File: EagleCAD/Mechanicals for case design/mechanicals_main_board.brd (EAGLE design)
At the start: 77 x 46.5 mm, 65 parts, among them Q1 DMC2700, U3 LM3676, U4 STM32F072-LQFP48, X1 32.768kHz

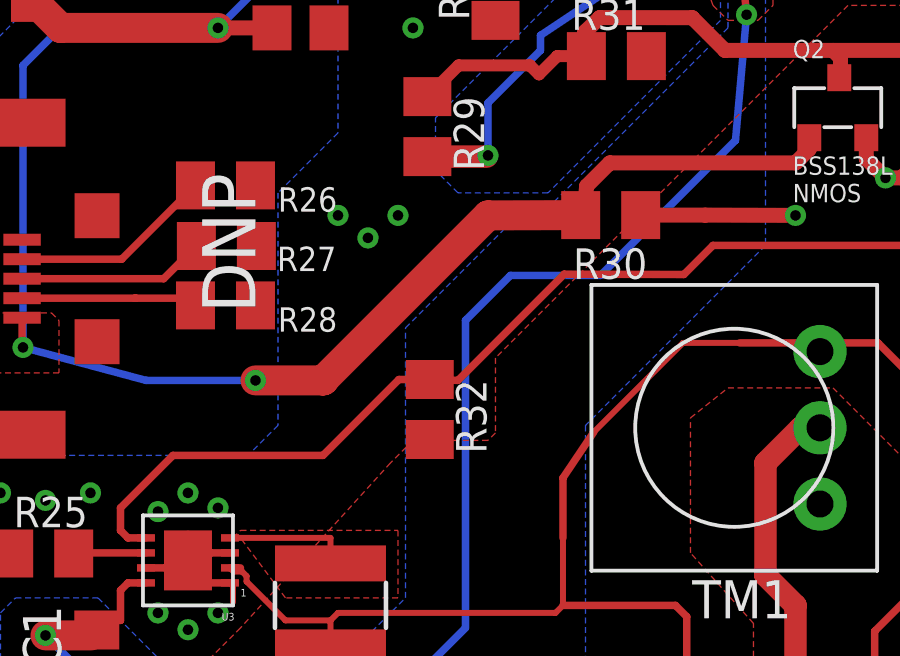
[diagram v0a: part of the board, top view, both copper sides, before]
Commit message: added basic mechanical drawings (no Z dimension) to allow beginning case design
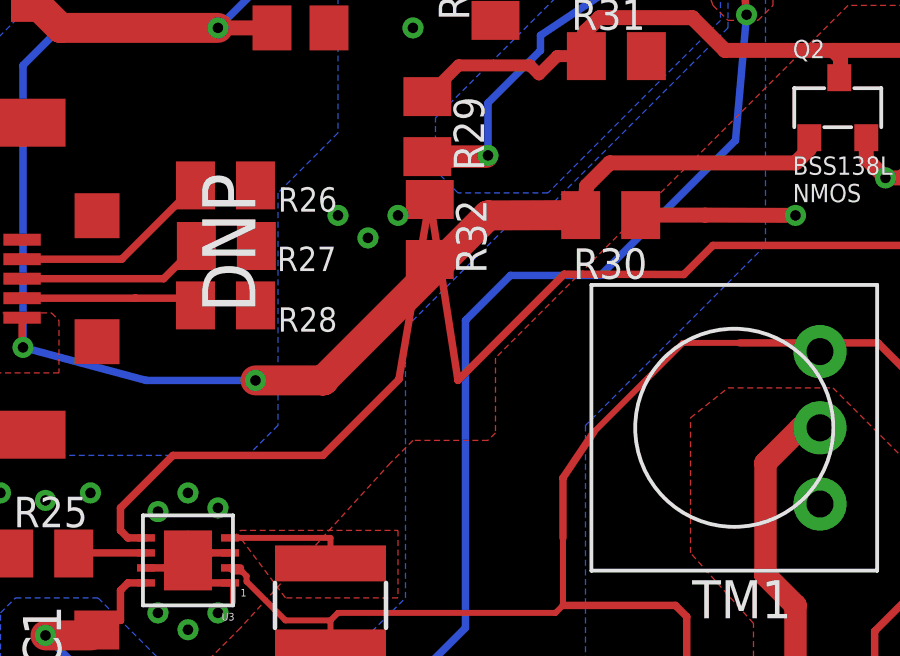
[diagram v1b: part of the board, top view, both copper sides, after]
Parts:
- moved R32 6.00 mm to (21.6, 19.5)
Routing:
- net BATT_CHG_LOGIC_OP: track 34.7 -> 44.9 mm
